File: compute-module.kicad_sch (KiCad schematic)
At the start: 0 parts

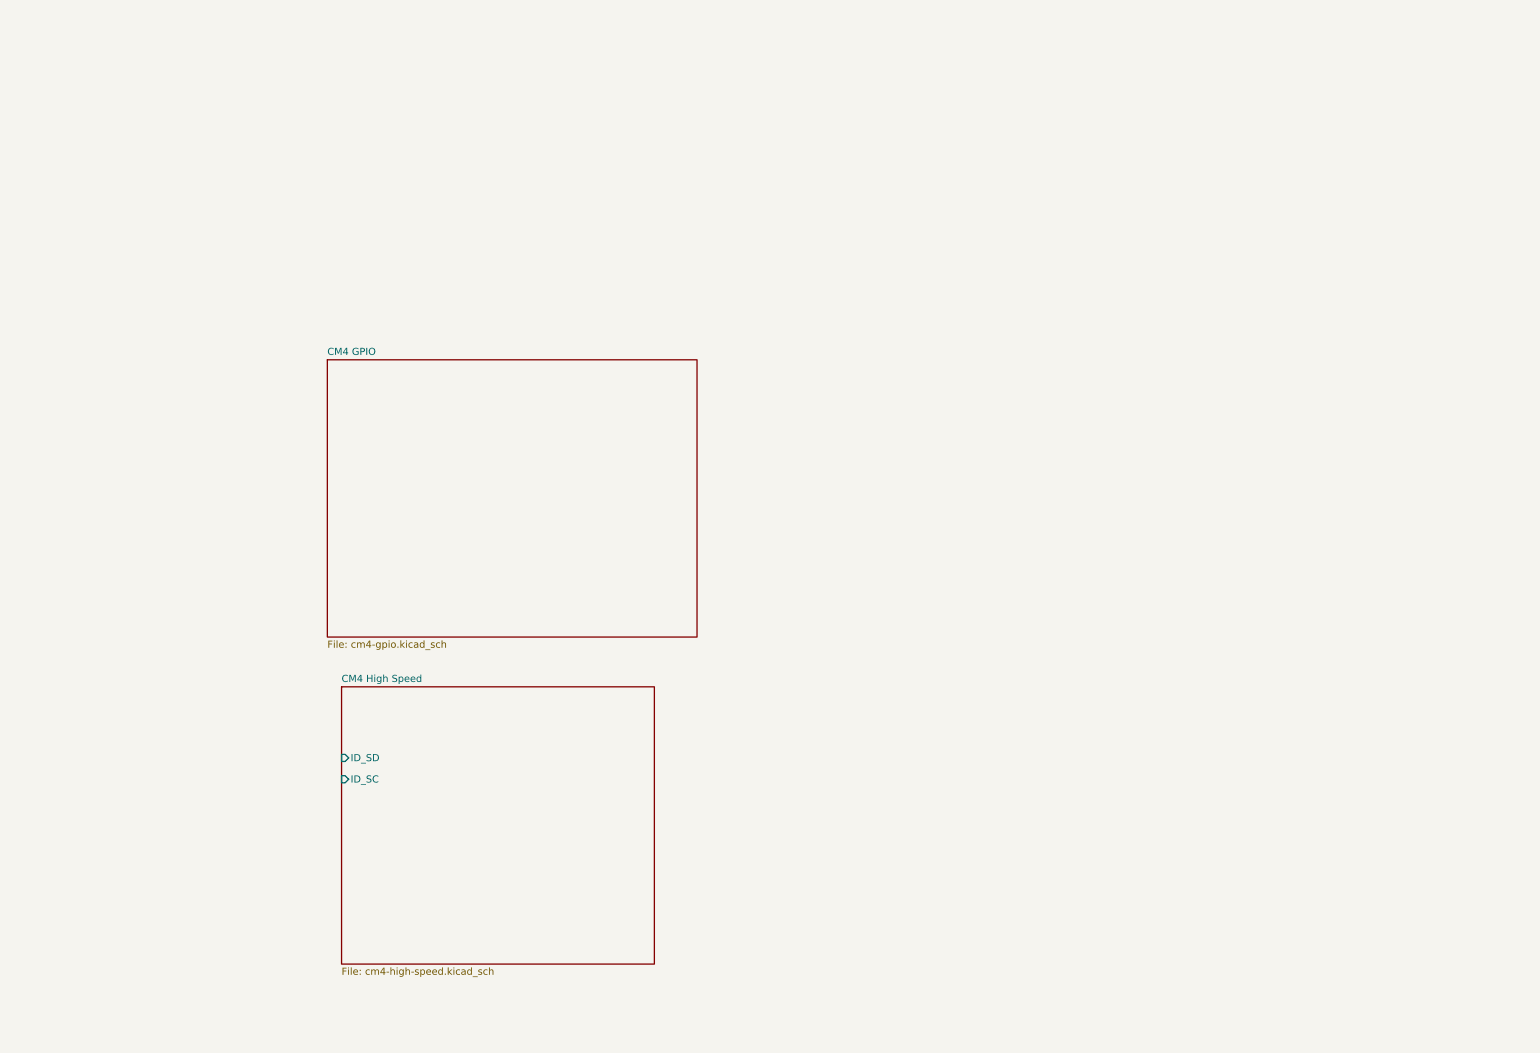
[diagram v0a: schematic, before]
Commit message: Unify CM4 sub-sheets.
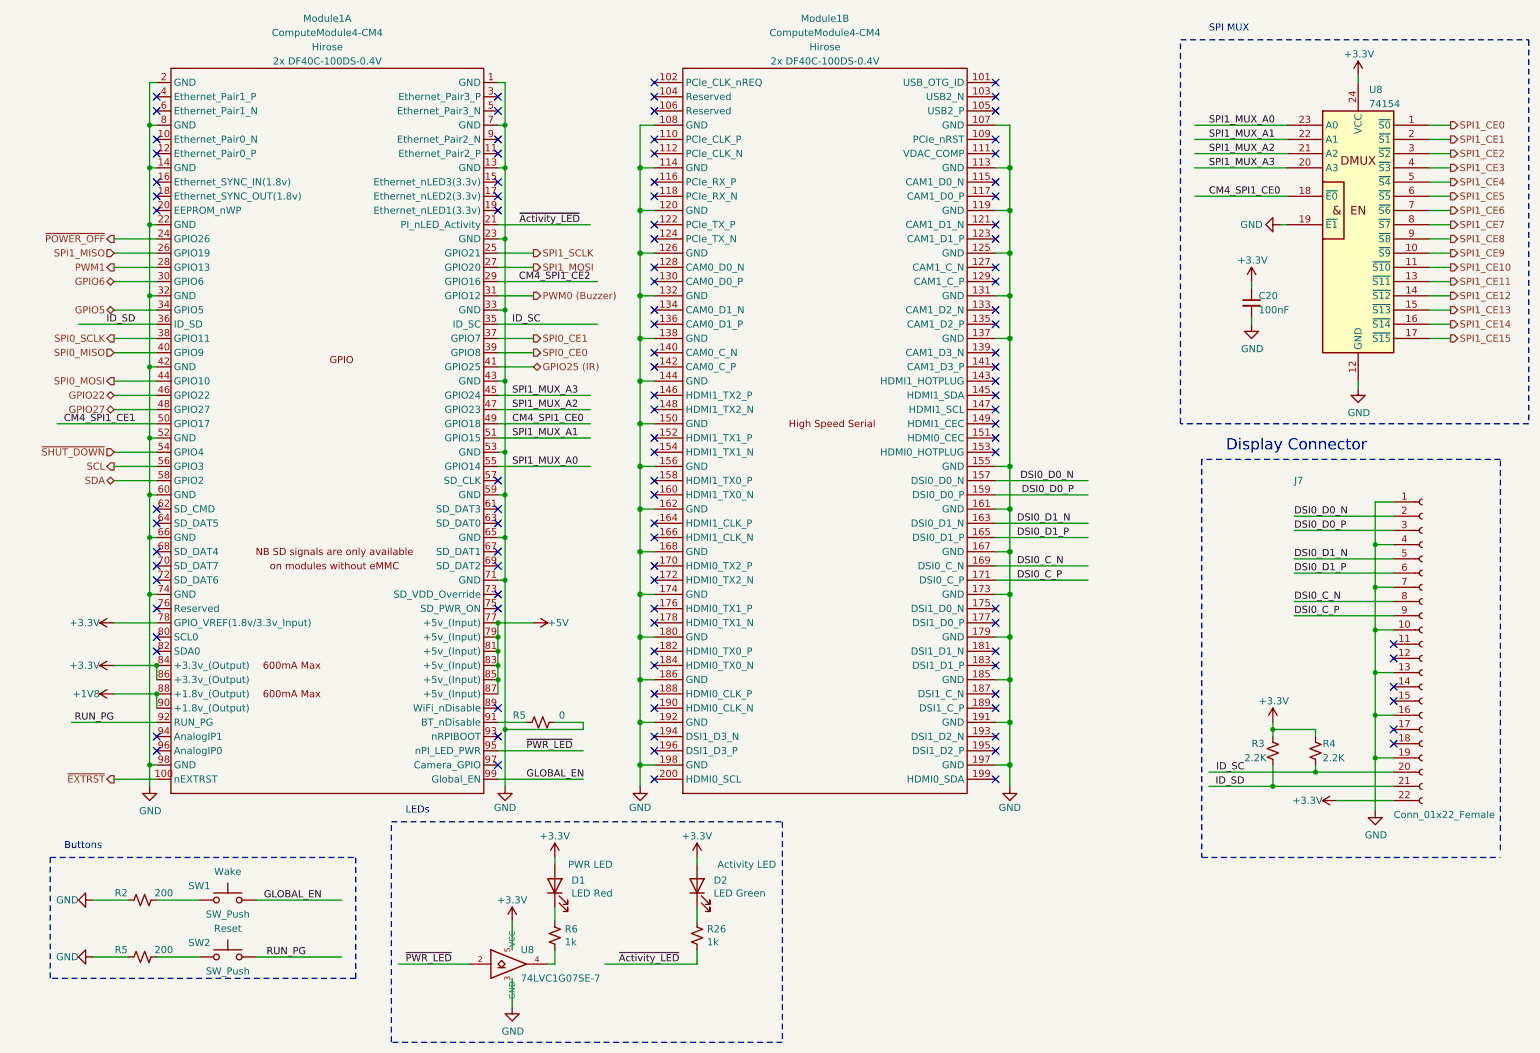
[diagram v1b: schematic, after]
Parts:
- added C20: 100nF, symbol Device:C_Small
- added D1: LED Red, LED_SMD:LED_0603_1608Metric, symbol Device:LED
- added D2: LED Green, LED_SMD:LED_0603_1608Metric, symbol Device:LED
- added J7: Conn_01x22_Female, FH12-22S:Hirose_FH12-22S-0.5SH_1x22-1MP_P0.50mm_Horizontal, symbol Connector:Conn_01x22_Female
- added Module1: ComputeModule4-CM4, rpi-cm4:rpi-cm4, symbol cm4:ComputeModule4-CM4
- added R2, R5: 200, symbol Device:R_Small_US
- added R26, R6: 1k, Resistor_SMD:R_0402_1005Metric, symbol Device:R_Small_US
- added R3, R4: 2.2K, Resistor_SMD:R_0402_1005Metric, symbol Device:R_Small_US
- added R5: 0, symbol Device:R_Small_US
- added SW1, SW2: SW_Push, symbol Switch:SW_Push
- added U8: 74LVC1G07SE-7, Package_TO_SOT_SMD:SOT-353_SC-70-5, symbol 74lvc1g07:74LVC1G07
- added U8: 74154, 74HC154:DHVQFN24, symbol 74xx_IEEE:74154
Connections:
- new net: R2.2, SW1.1
- new net: D2.1 (K), R26.1
- new net: R5.2, SW2.1
- new net: D1.1 (K), R6.1
- new net: R6.2, U8.4
- new net: Module1.91 (BT_nDisable), R5.1
- new net +1V8: Module1.88 (+1.8v_(Output)), Module1.90 (+1.8v_(Output))
- new net +3.3V: C20.1, D1.2 (A), D2.2 (A), J7.22 (Pin_22), Module1.78 (GPIO_VREF(1.8v/3.3v_Input)), Module1.84 (+3.3v_(Output)), Module1.86 (+3.3v_(Output)), R3.1, R4.1, U8.24 (VCC), U8.5 (VCC)
- new net +5V: Module1.77 (+5v_(Input)), Module1.79 (+5v_(Input)), Module1.81 (+5v_(Input)), Module1.83 (+5v_(Input)), Module1.85 (+5v_(Input)), Module1.87 (+5v_(Input))
- new net CM4_SPI1_CE0: Module1.49 (GPIO18), U8.18 (~{E0})
- new net CM4_SPI1_CE1: Module1.50 (GPIO17)
- new net CM4_SPI1_CE2: Module1.29 (GPIO16)
- new net DSI0_C_N: J7.8 (Pin_8), Module1.169 (DSI0_C_N)
- new net DSI0_C_P: J7.9 (Pin_9), Module1.171 (DSI0_C_P)
- new net DSI0_D0_N: J7.2 (Pin_2), Module1.157 (DSI0_D0_N)
- new net DSI0_D0_P: J7.3 (Pin_3), Module1.159 (DSI0_D0_P)
- new net DSI0_D1_N: J7.5 (Pin_5), Module1.163 (DSI0_D1_N)
- new net DSI0_D1_P: J7.6 (Pin_6), Module1.165 (DSI0_D1_P)
- new net GLOBAL_EN: Module1.99 (Global_EN), SW1.2
- new net GND: C20.2, J7.1 (Pin_1), J7.10 (Pin_10), J7.13 (Pin_13), J7.16 (Pin_16), J7.19 (Pin_19), J7.4 (Pin_4), J7.7 (Pin_7), Module1.1 (GND), Module1.107 (GND), Module1.108 (GND), Module1.113 (GND), Module1.114 (GND), Module1.119 (GND), Module1.120 (GND), Module1.125 (GND), Module1.126 (GND), Module1.13 (GND), Module1.131 (GND), Module1.132 (GND), Module1.137 (GND), Module1.138 (GND), Module1.14 (GND), Module1.144 (GND), Module1.150 (GND), Module1.155 (GND), Module1.156 (GND), Module1.161 (GND), Module1.162 (GND), Module1.167 (GND), Module1.168 (GND), Module1.173 (GND), Module1.174 (GND), Module1.179 (GND), Module1.180 (GND), Module1.185 (GND), Module1.186 (GND), Module1.191 (GND), Module1.192 (GND), Module1.197 (GND), Module1.198 (GND), Module1.2 (GND), Module1.22 (GND), Module1.23 (GND), Module1.32 (GND), Module1.33 (GND), Module1.42 (GND), Module1.43 (GND), Module1.52 (GND), Module1.53 (GND), Module1.59 (GND), Module1.60 (GND), Module1.65 (GND), Module1.66 (GND), Module1.7 (GND), Module1.71 (GND), Module1.74 (GND), Module1.8 (GND), Module1.98 (GND), R2.1, R5.1, R5.2, U8.12 (GND), U8.19 (~{E1}), U8.3 (GND)
- new net GPIO22: Module1.46 (GPIO22)
- new net GPIO25 (IR): Module1.41 (GPIO25)
- new net GPIO27: Module1.48 (GPIO27)
- new net GPIO5: Module1.34 (GPIO5)
- new net GPIO6: Module1.30 (GPIO6)
- new net ID_SC: J7.20 (Pin_20), Module1.35 (ID_SC), R4.2
- new net ID_SD: J7.21 (Pin_21), Module1.36 (ID_SD), R3.2
- new net PWM0 (Buzzer): Module1.31 (GPIO12)
- new net PWM1: Module1.28 (GPIO13)
- new net RUN_PG: Module1.92 (RUN_PG), SW2.2
- new net SCL: Module1.56 (GPIO3)
- new net SDA: Module1.58 (GPIO2)
- new net SPI0_CE0: Module1.39 (GPIO8)
- new net SPI0_CE1: Module1.37 (GPIO7)
- new net SPI0_MISO: Module1.40 (GPIO9)
- new net SPI0_MOSI: Module1.44 (GPIO10)
- new net SPI0_SCLK: Module1.38 (GPIO11)
- new net SPI1_CE0: U8.1 (~{S0})
- new net SPI1_CE1: U8.2 (~{S1})
- new net SPI1_CE10: U8.11 (~{S10})
- new net SPI1_CE11: U8.13 (~{S11})
- new net SPI1_CE12: U8.14 (~{S12})
- new net SPI1_CE13: U8.15 (~{S13})
- new net SPI1_CE14: U8.16 (~{S14})
- new net SPI1_CE15: U8.17 (~{S15})
- new net SPI1_CE2: U8.3 (~{S2})
- new net SPI1_CE3: U8.4 (~{S3})
- new net SPI1_CE4: U8.5 (~{S4})
- new net SPI1_CE5: U8.6 (~{S5})
- new net SPI1_CE6: U8.7 (~{S6})
- new net SPI1_CE7: U8.8 (~{S7})
- new net SPI1_CE8: U8.9 (~{S8})
- new net SPI1_CE9: U8.10 (~{S9})
- new net SPI1_MISO: Module1.26 (GPIO19)
- new net SPI1_MOSI: Module1.27 (GPIO20)
- new net SPI1_MUX_A0: Module1.55 (GPIO14), U8.23 (A0)
- new net SPI1_MUX_A1: Module1.51 (GPIO15), U8.22 (A1)
- new net SPI1_MUX_A2: Module1.47 (GPIO23), U8.21 (A2)
- new net SPI1_MUX_A3: Module1.45 (GPIO24), U8.20 (A3)
- new net SPI1_SCLK: Module1.25 (GPIO21)
- new net ~{Activity_LED}: Module1.21 (PI_nLED_Activity), R26.2
- new net ~{EXTRST}: Module1.100 (nEXTRST)
- new net ~{POWER_OFF}: Module1.24 (GPIO26)
- new net ~{PWR_LED}: Module1.95 (nPI_LED_PWR), U8.2
- new net ~{SHUT_DOWN}: Module1.54 (GPIO4)
- no-connect marks 0 -> 104
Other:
- removed sheet CM4 GPIO
- removed sheet CM4 High Speed
- note added: "Buttons"
- note added: "Display Connector"
- note added: "LEDs"
- note added: "SPI MUX"

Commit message: Add RP2040
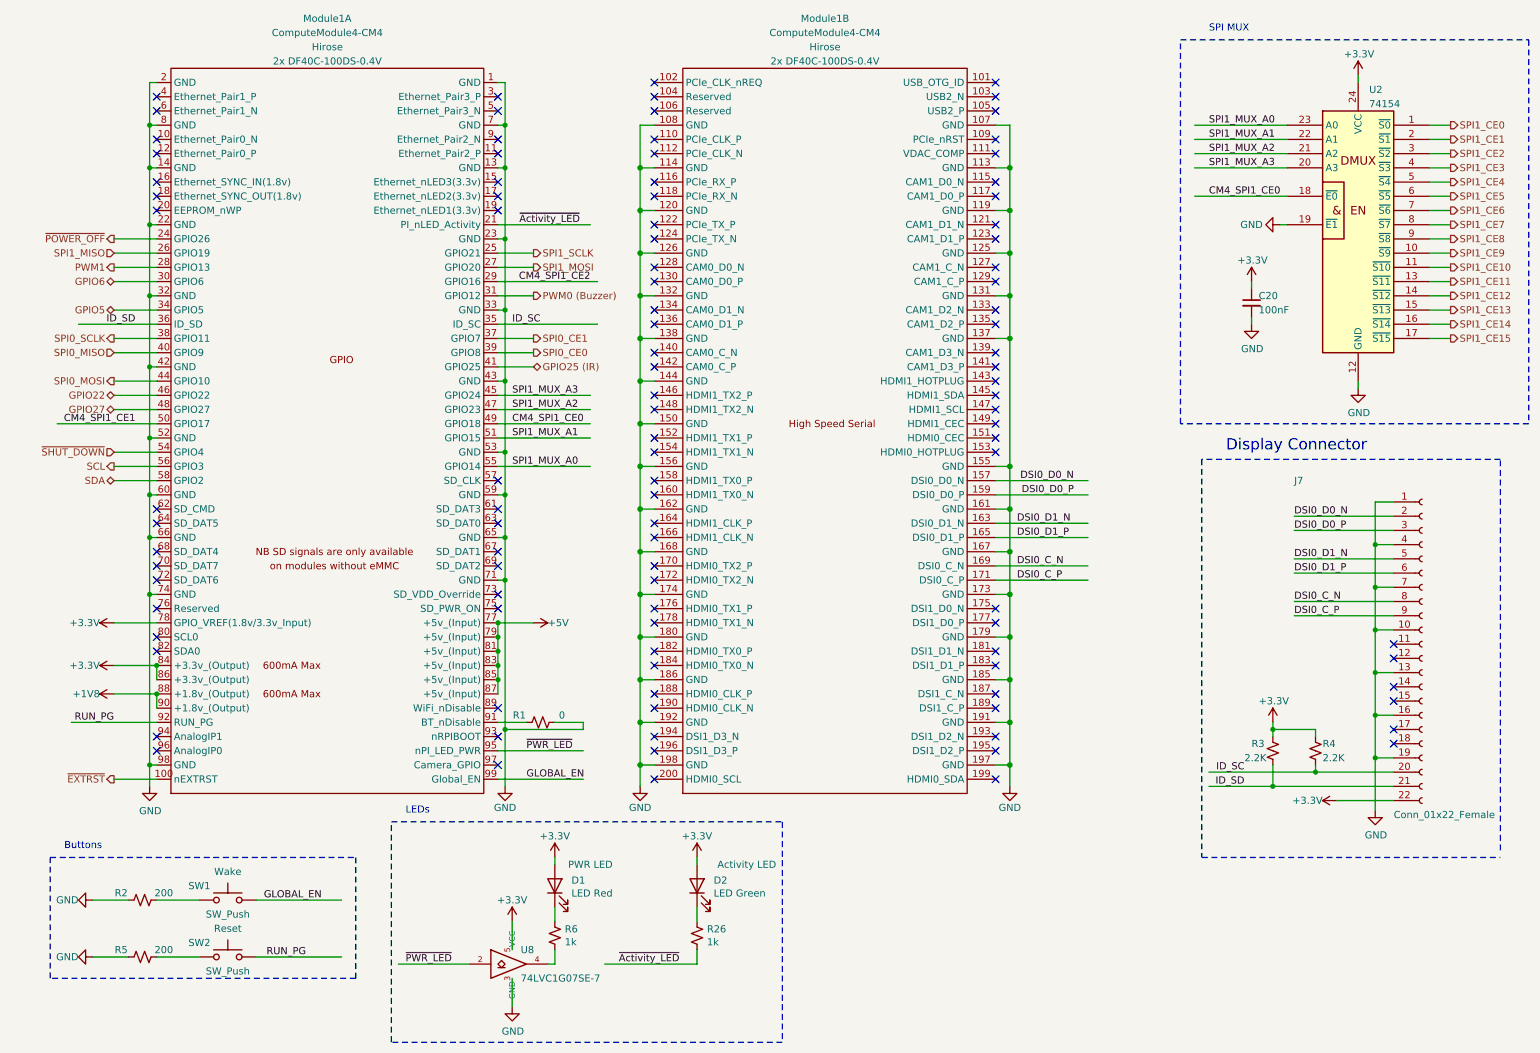
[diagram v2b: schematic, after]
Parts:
- renumbered R5 to R1, U8 to U2
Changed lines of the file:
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@@
   (symbol (lib_id "power:+3.3V") (at 233.68 139.7 0) (unit 1)
     (in_bom yes) (on_board yes) (dnp no)
-    (property "Reference" "#PWR015" (at 233.68 143.51 0)
+    (property "Reference" "#PWR010" (at 233.68 143.51 0)
       (effects (font (size 1.27 1.27)) hide)
     )
@@
   (symbol (lib_id "power:+3.3V") (at 130.81 163.83 0) (unit 1)
     (in_bom yes) (on_board yes) (dnp no) (fields_autoplaced)
-    (property "Reference" "#PWR016" (at 130.81 167.64 0)
+    (property "Reference" "#PWR059" (at 130.81 167.64 0)
       (effects (font (size 1.27 1.27)) hide)
     )
@@
   (symbol (lib_id "power:+3.3V") (at 26.67 121.92 90) (unit 1)
     (in_bom yes) (on_board yes) (dnp no)
-    (property "Reference" "#PWR015" (at 30.48 121.92 0)
+    (property "Reference" "#PWR03" (at 30.48 121.92 0)
       (effects (font (size 1.27 1.27)) hide)
     )
@@
   (symbol (lib_id "power:+3.3V") (at 26.67 129.54 90) (unit 1)
     (in_bom yes) (on_board yes) (dnp no)
-    (property "Reference" "#PWR09" (at 30.48 129.54 0)
+    (property "Reference" "#PWR04" (at 30.48 129.54 0)
       (effects (font (size 1.27 1.27)) hide)
     )
@@
   (symbol (lib_id "power:+3.3V") (at 97.79 175.26 0) (unit 1)
     (in_bom yes) (on_board yes) (dnp no) (fields_autoplaced)
-    (property "Reference" "#PWR08" (at 97.79 179.07 0)
+    (property "Reference" "#PWR056" (at 97.79 179.07 0)
       (effects (font (size 1.27 1.27)) hide)
     )
@@
   (symbol (lib_id "power:+5V") (at 101.6 121.92 270) (unit 1)
     (in_bom yes) (on_board yes) (dnp no)
-    (property "Reference" "#PWR011" (at 97.79 121.92 0)
+    (property "Reference" "#PWR09" (at 97.79 121.92 0)
       (effects (font (size 1.27 1.27)) hide)
     )
@@
   (symbol (lib_id "power:+3.3V") (at 105.41 163.83 0) (unit 1)
     (in_bom yes) (on_board yes) (dnp no) (fields_autoplaced)
-    (property "Reference" "#PWR013" (at 105.41 167.64 0)
+    (property "Reference" "#PWR058" (at 105.41 167.64 0)
       (effects (font (size 1.27 1.27)) hide)
     )
@@
   (symbol (lib_id "power:+3.3V") (at 248.92 24.13 0) (unit 1)
     (in_bom yes) (on_board yes) (dnp no)
-    (property "Reference" "#PWR056" (at 248.92 27.94 0)
+    (property "Reference" "#PWR016" (at 248.92 27.94 0)
       (effects (font (size 1.27 1.27)) hide)
     )
@@
   (symbol (lib_id "power:GND") (at 251.968 155.448 0) (unit 1)
     (in_bom yes) (on_board yes) (dnp no)
-    (property "Reference" "#PWR010" (at 251.968 161.798 0)
+    (property "Reference" "#PWR055" (at 251.968 161.798 0)
       (effects (font (size 1.27 1.27)) hide)
     )
@@
   (symbol (lib_id "74xx_IEEE:74154") (at 248.92 53.34 0) (unit 1)
     (in_bom yes) (on_board yes) (dnp no) (fields_autoplaced)
-    (property "Reference" "U8" (at 250.8759 26.67 0)
+    (property "Reference" "U2" (at 250.8759 26.67 0)
       (effects (font (size 1.27 1.27)) (justify left))
     )
@@
   (symbol (lib_id "power:+3.3V") (at 245.11 153.67 90) (unit 1)
     (in_bom yes) (on_board yes) (dnp no)
-    (property "Reference" "#PWR015" (at 248.92 153.67 0)
+    (property "Reference" "#PWR054" (at 248.92 153.67 0)
       (effects (font (size 1.27 1.27)) hide)
     )
@@
   (symbol (lib_id "power:+1V8") (at 26.67 134.62 90) (unit 1)
     (in_bom yes) (on_board yes) (dnp no)
-    (property "Reference" "#PWR014" (at 30.48 134.62 0)
+    (property "Reference" "#PWR05" (at 30.48 134.62 0)
       (effects (font (size 1.27 1.27)) hide)
     )
@@
   (symbol (lib_id "power:+3.3V") (at 229.87 60.96 0) (unit 1)
     (in_bom yes) (on_board yes) (dnp no)
-    (property "Reference" "#PWR058" (at 229.87 64.77 0)
+    (property "Reference" "#PWR013" (at 229.87 64.77 0)
       (effects (font (size 1.27 1.27)) hide)
     )
@@
   (symbol (lib_id "Device:R_Small_US") (at 102.87 139.7 90) (unit 1)
     (in_bom yes) (on_board yes) (dnp no)
-    (property "Reference" "R5" (at 99.06 138.43 90)
-      (effects (font (size 1.27 1.27)))
-    )
+    (property "Reference" "R1" (at 99.06 138.43 90)
+      (effects (font (size 1.27 1.27)))
+    )
